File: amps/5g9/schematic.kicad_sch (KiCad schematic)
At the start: 68 parts, among them T1 8160, T2 108

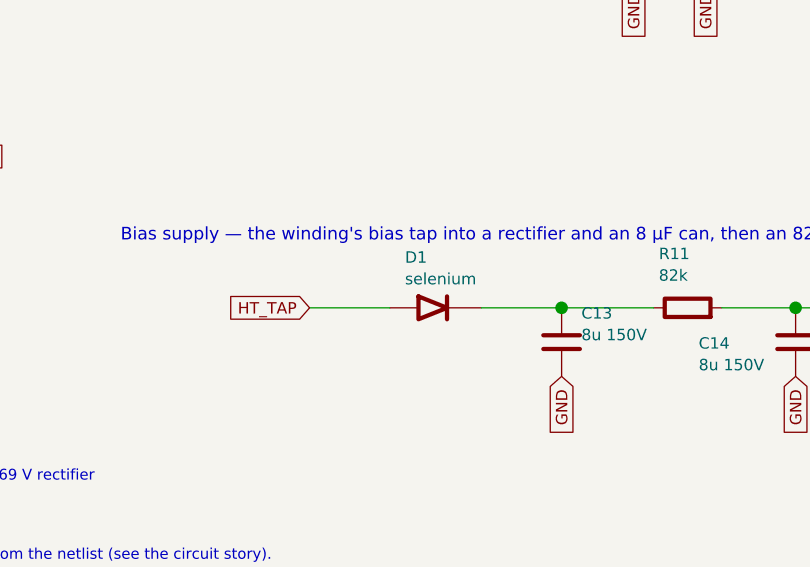
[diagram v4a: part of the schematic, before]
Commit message: Fix: 17 bias rectifiers and six HT diodes drawn backwards; the 6G6-B and 6G4 bias rows as their drawings show; AA1164 V4 units
Rectifier polarity has no gate. The netlists model every supply as an ideal
source, the sheet-vs-board check treats a two-terminal part as unordered, and
the boards' `cathode:` fields were copied from the sheets. Measured over all
68 diodes on 40 sheets: 18 negative-bias rectifiers had the cathode on the
negative node (a diode that way round would charge the node POSITIVE), and all
six 6G6-B HT diodes pointed away from B+. The printed negative bias on each of
those sheets falsifies the drawn orientation; the nine bias rectifiers already
right (AA1164, AA864, AB165, B15N, DR103, JTM100, M1959, M2204, 6G6-B) show
the idiom. Flipped: 5E4-A, 5E5-A, 5E6-A, 5F10, 5F4, 5F6, 5F6-A, 5F8-A, 5G9,
6G2, 6G3, 6G4, 6G5, AA964, AB763, AB763 Super, AB763 Twin, JTM45 (the
M1987's is with the Marshall board repair) and the 6G6-B's DR1-DR6. The
5F8-A board, which had copied its sheet, has the band moved to the tap side;
the other boards' bands are with the board-repair wave. A gate is next.

6G6-B bias. E-FB (6431x3364): the 1K 1W rises from TR1's SECOND secondary
terminal, a bias tap between the upper HT end and the grounded centre tap,
to the diode's + end. The sheet fed the diode from the HT end with the 1K
after it. T1 now carries its tap pin and the row reads tap -> 1K -> diode ->
-54 V. (The triage had read "HT end"; the native crop shows the tap.)

6G4 bias. A-FJ, read natively: tap -> rectifier -> 8 uF -> 10K -> the -55 V
node, which carries a second 8 uF and the 56K to ground as a bleeder. The
sheet fed the rectifier from an HT end, drew the 56K in series and carried
one capacitor. CBIAS2 joins the parts list, and RBIAS1's role now says
bleeder.

AA1164 V4. The K-FD sheet prints the phase inverter 7/6/8 and the tremolo
oscillator 2/1/3 (5554x4346); the sheet had them the other way round.

Gates: check_schematics 40/0 (+selftest), verify_schematic_nets 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
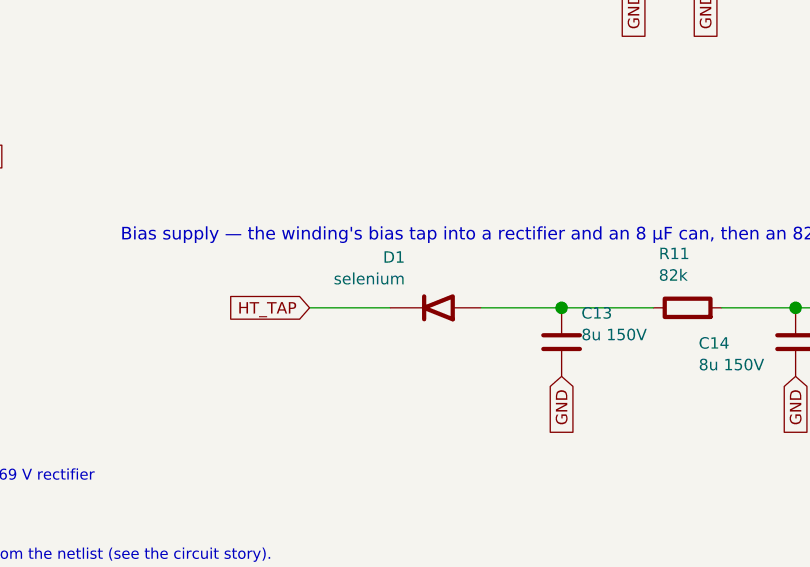
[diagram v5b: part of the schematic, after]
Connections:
- net HT_TAP: now also D1.2 (K); no longer D1.1 (A)
- net at C13.1, R11.1: now also D1.1 (A); no longer D1.2 (K)
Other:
- moved on the sheet: D1
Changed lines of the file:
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@@
   (wire (pts (xy 247.609 233.75) (xy 256.529 233.75))
     (stroke (width 0) (type default)))
-  (symbol (lib_id "cx:DIODE_SS") (at 261.609 233.75 0) (unit 1)
+  (symbol (lib_id "cx:DIODE_SS") (at 261.609 233.75 180) (unit 1)
     (in_bom yes) (on_board yes)
     (property "Reference" "D1" (at 258.209 228.15 0) (effects (font (size 1.27 1.27)) (justify left)))

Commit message: Fix: the 6G5's rectifier was connected to nothing; 17 sheets shorted the mains by naming both leads alike
6G5 power supply. The sheet drew four diodes as a "silicon bridge" whose
HT_A/HT_B labels stopped 6 mm short of their wires. D1/D2's anodes sat on
the tremolo's cathode node (a tremolo wire's end touched the old diode
stub), D3/D4 ran from ground to the reservoir, and TR1's centre tap floated
under an open-pin waiver whose stated reason was the bridge itself.
A-FJ (Schematic Heaven 2153x1437, read enlarged): each HT end of TR1 runs
through a leg of three silicon diodes, every + (cathode) toward the +460 V
reservoir; the centre tap is grounded; TR1's second secondary terminal is a
bias tap feeding the 6G4's network part for part: rectifier, 8-150, 10K,
then 8-150 and a 56K bleeder at the -55 V line. Redrawn as the drawing
shows: D1-D6, TR1 with its tap pin, the centre tap to ground, the bias
network (CBIAS 25 uF -> 8 uF; RBIAS2, CBIAS2, RBIAS1 added), the waiver
deleted, and the notes, meta, netlist header and parts list no longer say
bridge. Not yet carried: the drawing's second 20-600 at the reservoir and
the standby switch (this sheet omits chassis switches by its own note);
and the tremolo ladder still runs through the transformer's corner of the
sheet, a layout clash rather than a connection, queued for its own redraw.

Mains. Two global labels with one name are one net. 16 of 24 power
transformers on the sheets carried a label named MAINS on both primary
leads, so the winding's two pins were one net: 5E4-A, 5E5-A, 5F4, 5G9,
6161, 6G2, 6G3, 6G4, AA1164, AA764, AA764-Vibro, AA964, AB763, AB763
Super, AB763 Twin, GA-40. The 6G5's loop ran from one MAINS label through
switch, fuse and winding back to the same name. No gate models the primary,
so a copy-pasted idiom did this. The second lead is now MAINS N, the AC15's
idiom; the AA1164's and AA964's second AC row, drawn under the first row's
name, is the neutral. The death and across-the-line caps stay on the le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
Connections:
- net MAINS: no longer T1.2 (PRI_2)
- new net MAINS N: T1.2 (PRI_2)
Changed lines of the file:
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@@
   (wire (pts (xy 222.719 188.83) (xy 218.719 188.83))
     (stroke (width 0) (type default)))
-  (global_label "MAINS" (shape input) (at 218.719 188.83 180)
+  (global_label "MAINS N" (shape input) (at 218.719 188.83 180)
     (effects (font (size 1.27 1.27)) (justify right)))
   (wire (pts (xy 240.499 178.67) (xy 250.499 178.67))
